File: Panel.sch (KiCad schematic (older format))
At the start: 10 parts, among them J6 Rotated_Barrel, U7 LM3406HV

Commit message: Added Component-Associations (about 10% remaining)
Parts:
- C20: Buy https://www.digikey.com/product-detail/en/samsung-electro-m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 -> (none)
- C21, C23: Buy https://www.digikey.com/product-detail/en/samsung-electro-m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 -> https://www.digikey.com/product-detail/en/kemet/C0603C104M5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
- C22: Buy https://www.digikey.com/product-detail/en/kemet/C0805C223K5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 -> https://www.digikey.com/product-detail/en/kemet/C0603C223K1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
- R11: Buy https://www.digikey.com/product-detail/en/yageo/RC0805FR-07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 -> https://www.digikey.com/product-detail/en/yageo/RC0603FR-07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
- R12: footprint Resistors_SMD:R_0603 -> Resistors_SMD:R_0805
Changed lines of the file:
@@
 $Descr A4 11693 8268
 encoding utf-8
-Sheet 4 7
+Sheet 3 7
 Title ""
 Date "2018-02-14"
@@
 AR Path="/5A4C34AF/5A7753B7" Ref="R11"  Part="1"
 AR Path="/5A4C3F5F/5A7753B7" Ref="R13"  Part="1"
-F 0 "R13" V 1430 1300 50  0000 C CNN
+F 0 "R11" V 1430 1300 50  0000 C CNN
 F 1 "162k" V 1350 1300 50  0000 C CNN
 F 2 "Resistors_SMD:R_0603" V 1280 1300 50  0001 C CNN
 F 3 "" H 1350 1300 50  0001 C CNN
-F 4 "https://www.digikey.com/product-detail/en/yageo/RC0805FR-07162KL/311-162KCRCT-ND/730577" V 1350 1300 60  0001 C CNN "Buy"
+F 4 "https://www.digikey.com/product-detail/en/yageo/RC0603FR-07162KL/311-162KHRCT-ND/729922" V 1350 1300 50  0001 C CNN "Buy"
 	1    1350 1300
 	1    0    0    -1
@@
 AR Path="/5A4C34AF/5A77745B" Ref="C21"  Part="1"
 AR Path="/5A4C3F5F/5A77745B" Ref="C25"  Part="1"
-F 0 "C25" H 1510 2220 50  0000 L CNN
+F 0 "C21" H 1510 2220 50  0000 L CNN
 F 1 "100nF" H 1510 2070 50  0000 L CNN
 F 2 "Capacitors_SMD:C_0603" H 1500 2150 50  0001 C CNN
 F 3 "" H 1500 2150 50  0001 C CNN
-F 4 "https://www.digikey.com/product-detail/en/samsung-electro-mechanics/CL21B104KACNNNC/1276-1099-1-ND/3889185" H 1500 2150 60  0001 C CNN "Buy"
+F 4 "https://www.digikey.com/product-detail/en/kemet/C0603C104M5RACTU/399-7845-1-ND/3471568" H 1500 2150 60  0001 C CNN "Buy"
 	1    1500 2150
 	1    0    0    -1
@@
 AR Path="/5A4C34AF/5A777BDD" Ref="#PWR061"  Part="1"
 AR Path="/5A4C3F5F/5A777BDD" Ref="#PWR068"  Part="1"
-F 0 "#PWR068" H 1500 2050 50  0001 C CNN
+F 0 "#PWR061" H 1500 2050 50  0001 C CNN
 F 1 "GND" H 1500 2150 50  0000 C CNN
 F 2 "" H 1500 2300 50  0001 C CNN
@@
 AR Path="/5A4C34AF/5A777CD4" Ref="C23"  Part="1"
 AR Path="/5A4C3F5F/5A777CD4" Ref="C27"  Part="1"
-F 0 "C27" H 2710 2220 50  0000 L CNN
+F 0 "C23" H 2710 2220 50  0000 L CNN
 F 1 "100nF" H 2710 2070 50  0000 L CNN
 F 2 "Capacitors_SMD:C_0603" H 2700 2150 50  0001 C CNN
 F 3 "" H 2700 2150 50  0001 C CNN
-F 4 "https://www.digikey.com/product-detail/en/samsung-electro-mechanics/CL21B104KACNNNC/1276-1099-1-ND/3889185" H 2700 2150 60  0001 C CNN "Buy"
+F 4 "https://www.digikey.com/product-detail/en/kemet/C0603C104M5RACTU/399-7845-1-ND/3471568" H 2700 2150 50  0001 C CNN "Buy"
 	1    2700 2150
 	1    0    0    -1
@@
 AR Path="/5A4C34AF/5A777CDA" Ref="#PWR063"  Part="1"
 AR Path="/5A4C3F5F/5A777CDA" Ref="#PWR070"  Part="1"
-F 0 "#PWR070" H 2700 2050 50  0001 C CNN
+F 0 "#PWR063" H 2700 2050 50  0001 C CNN
 F 1 "GND" H 2700 2150 50  0000 C CNN
 F 2 "" H 2700 2300 50  0001 C CNN
@@
 AR Path="/5A4C34AF/5A777FA3" Ref="#PWR062"  Part="1"
 AR Path="/5A4C3F5F/5A777FA3" Ref="#PWR069"  Part="1"
-F 0 "#PWR069" H 2100 2050 50  0001 C CNN
+F 0 "#PWR062" H 2100 2050 50  0001 C CNN
 F 1 "GND" H 2100 2150 50  0000 C CNN
 F 2 "" H 2100 2300 50  0001 C CNN
@@
 AR Path="/5A4C34AF/5A77816D" Ref="C22"  Part="1"
 AR Path="/5A4C3F5F/5A77816D" Ref="C26"  Part="1"
-F 0 "C26" H 2460 920 50  0000 L CNN
+F 0 "C22" H 2460 920 50  0000 L CNN
 F 1 "22nF" H 2460 770 50  0000 L CNN
 F 2 "Capacitors_SMD:C_0603" H 2450 850 50  0001 C CNN
 F 3 "" H 2450 850 50  0001 C CNN
-F 4 "https://www.digikey.com/product-detail/en/kemet/C0805C223K5RACTU/399-1163-1-ND/411438" H 2450 850 60  0001 C CNN "Buy"
+F 4 "https://www.digikey.com/product-detail/en/kemet/C0603C223K1RACTU/399-3476-1-ND/754769" H 2450 850 50  0001 C CNN "Buy"
 	1    2450 850
 	0    -1   -1   0
@@
 AR Path="/5A4C34AF/5A77899A" Ref="L3"  Part="1"
 AR Path="/5A4C3F5F/5A77899A" Ref="L4"  Part="1"
-F 0 "L4" V 3200 1050 50  0000 C CNN
+F 0 "L3" V 3200 1050 50  0000 C CNN
 F 1 "33μH" V 3325 1050 50  0000 C CNN
 F 2 "" H 3250 1050 50  0001 C CNN
@@
 AR Path="/5A4C34AF/5A7789F9" Ref="D1"  Part="1"
 AR Path="/5A4C3F5F/5A7789F9" Ref="D2"  Part="1"
-F 0 "D2" H 3000 1400 50  0000 C CNN
+F 0 "D1" H 3000 1400 50  0000 C CNN
 F 1 "D_Schot" H 2950 1200 50  0000 C CNN
 F 2 "Diodes_SMD:D_SOD-123" H 3000 1300 50  0001 C CNN
@@
 AR Path="/5A4C34AF/5A778B62" Ref="#PWR064"  Part="1"
 AR Path="/5A4C3F5F/5A778B62" Ref="#PWR071"  Part="1"
-F 0 "#PWR071" H 3000 2050 50  0001 C CNN
+F 0 "#PWR064" H 3000 2050 50  0001 C CNN
 F 1 "GND" H 3000 2150 50  0000 C CNN
 F 2 "" H 3000 2300 50  0001 C CNN
@@
 AR Path="/5A4C34AF/5A779AD3" Ref="J6"  Part="1"
 AR Path="/5A4C3F5F/5A779AD3" Ref="J7"  Part="1"
-F 0 "J7" H 3700 1710 50  0000 C CNN
+F 0 "J6" H 3700 1710 50  0000 C CNN
 F 1 "Rotated_Barrel" H 3750 1350 50  0000 C CNN
 F 2 "Connectors:BARREL_JACK" H 3750 1440 50  0001 C CNN
@@
 AR Path="/5A4C34AF/5A77A2E1" Ref="R12"  Part="1"
 AR Path="/5A4C3F5F/5A77A2E1" Ref="R14"  Part="1"
-F 0 "R14" V 3530 1900 50  0000 C CNN
+F 0 "R12" V 3530 1900 50  0000 C CNN
 F 1 "0R16" V 3450 1900 50  0000 C CNN
-F 2 "Resistors_SMD:R_0603" V 3380 1900 50  0001 C CNN
+F 2 "Resistors_SMD:R_0805" V 3380 1900 50  0001 C CNN
 F 3 "" H 3450 1900 50  0001 C CNN
 F 4 "https://www.digikey.com/product-detail/en/panasonic-electronic-components/ERJ-6DSFR16V/P19313CT-ND/6004668" V 3450 1900 60  0001 C CNN "Buy"
@@
 AR Path="/5A4C34AF/5A77A9CB" Ref="#PWR065"  Part="1"
 AR Path="/5A4C3F5F/5A77A9CB" Ref="#PWR072"  Part="1"
-F 0 "#PWR072" H 3450 2050 50  0001 C CNN
+F 0 "#PWR065" H 3450 2050 50  0001 C CNN
 F 1 "GND" H 3450 2150 50  0000 C CNN
 F 2 "" H 3450 2300 50  0001 C CNN
@@
 AR Path="/5A4C34AF/5A77D10E" Ref="C20"  Part="1"
 AR Path="/5A4C3F5F/5A77D10E" Ref="C24"  Part="1"
-F 0 "C24" H 1110 1370 50  0000 L CNN
+F 0 "C20" H 1110 1370 50  0000 L CNN
 F 1 "1μF" H 1110 1220 50  0000 L CNN
 F 2 "Capacitors_SMD:C_0603" H 1100 1300 50  0001 C CNN
 F 3 "" H 1100 1300 50  0001 C CNN
-F 4 "https://www.digikey.com/product-detail/en/samsung-electro-mechanics/CL31B105KCHNNNE/1276-1838-1-ND/3889924" H 1100 1300 60  0001 C CNN "Buy"
 	1    1100 1300
 	1    0    0    -1
@@
 AR Path="/5A4C34AF/5A77D43C" Ref="#PWR060"  Part="1"
 AR Path="/5A4C3F5F/5A77D43C" Ref="#PWR067"  Part="1"
-F 0 "#PWR067" H 1100 2050 50  0001 C CNN
+F 0 "#PWR060" H 1100 2050 50  0001 C CNN
 F 1 "GND" H 1100 2150 50  0000 C CNN
 F 2 "" H 1100 2300 50  0001 C CNN
@@
 AR Path="/5A4C34AF/5A77E620" Ref="U7"  Part="1"
 AR Path="/5A4C3F5F/5A77E620" Ref="U8"  Part="1"
-F 0 "U8" H 2500 950 60  0000 C CNN
+F 0 "U7" H 2500 950 60  0000 C CNN
 F 1 "LM3406HV" H 1900 2050 60  0000 C CNN
 F 2 "Housings_SSOP:TSSOP-14_4.4x5mm_Pitch0.65mm" H 2100 2100 60  0001 C CNN
@@
 AR Path="/5A4C34AF/5A84C99A" Ref="#PWR059"  Part="1"
 AR Path="/5A4C3F5F/5A84C99A" Ref="#PWR066"  Part="1"
-F 0 "#PWR066" H 1050 800 50  0001 C CNN
+F 0 "#PWR059" H 1050 800 50  0001 C CNN
 F 1 "+48V" H 1050 1090 50  0000 C CNN
 F 2 "" H 1050 950 50  0001 C CNN

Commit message: Minor changes to layout and component association
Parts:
- C21, C23: Buy https://www.digikey.com/product-detail/en/kemet/C0603C104M5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 -> https://www.digikey.com/product-detail/en/kemet/C0603C104K3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
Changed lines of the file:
@@
 F 2 "Capacitors_SMD:C_0603" H 1500 2150 50  0001 C CNN
 F 3 "" H 1500 2150 50  0001 C CNN
-F 4 "https://www.digikey.com/product-detail/en/kemet/C0603C104M5RACTU/399-7845-1-ND/3471568" H 1500 2150 60  0001 C CNN "Buy"
+F 4 "https://www.digikey.com/product-detail/en/kemet/C0603C104K3RACTU/399-1281-1-ND/416057" H 1500 2150 60  0001 C CNN "Buy"
 	1    1500 2150
 	1    0    0    -1
@@
 F 2 "Capacitors_SMD:C_0603" H 2700 2150 50  0001 C CNN
 F 3 "" H 2700 2150 50  0001 C CNN
-F 4 "https://www.digikey.com/product-detail/en/kemet/C0603C104M5RACTU/399-7845-1-ND/3471568" H 2700 2150 50  0001 C CNN "Buy"
+F 4 "https://www.digikey.com/product-detail/en/kemet/C0603C104K3RACTU/399-1281-1-ND/416057" H 2700 2150 50  0001 C CNN "Buy"
 	1    2700 2150
 	1    0    0    -1

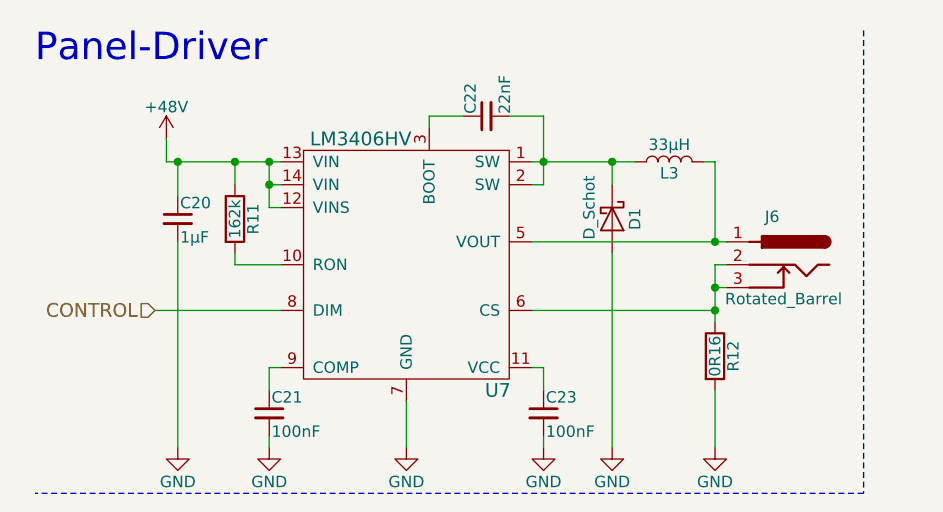
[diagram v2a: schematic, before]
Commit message: Added about 8% of the remaining components
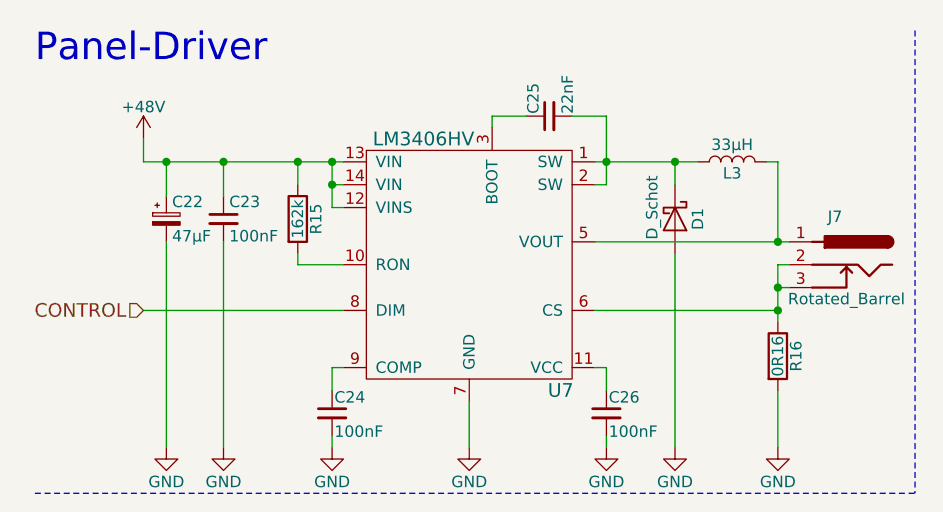
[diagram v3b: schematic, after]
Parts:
- removed C20: 1μF, Capacitors_SMD:C_0603, symbol Device:C_Small
- added C22: 47μF, symbol Device:CP_Small
- added C23: 100nF, Capacitor_SMD:C_0805_2012Metric, symbol Device:C_Small
- D1: footprint Diodes_SMD:D_SOD-123 -> Diode_SMD:D_SMA_Handsoldering; Buy https://www.digikey.com/product-detail/en/nexperia-usa-inc/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 -> https://www.digikey.com/product-detail/en/smc-diode-solutio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
- renumbered C21 to C24, C22 to C25, C23 to C26, J6 to J7, R11 to R15, R12 to R16
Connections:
- net +48V: now also C22.1, C23.1
- net GND: now also C22.2, C23.2
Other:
- moved on the sheet: C24, C25, C26, D1, J7, L3, R15, R16, U7

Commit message: Added Gate Pull-Downs
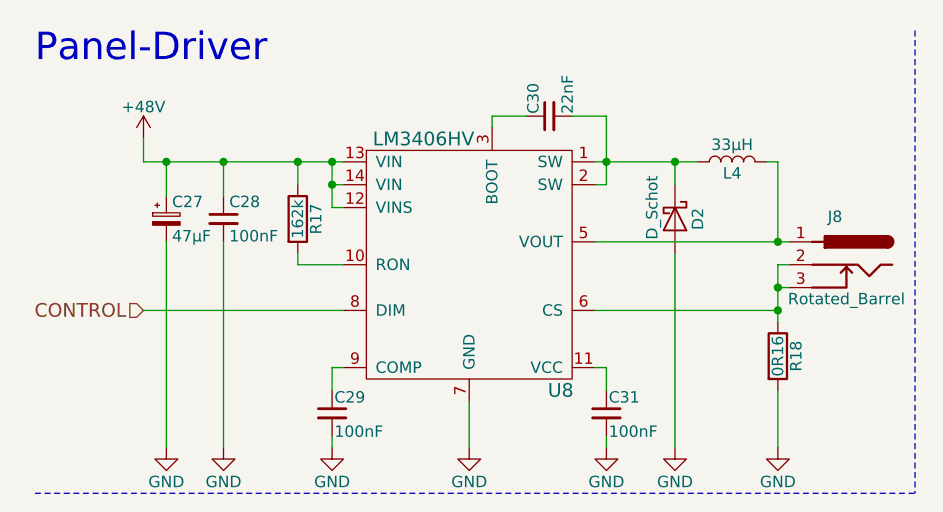
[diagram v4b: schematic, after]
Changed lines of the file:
@@
 $Descr A4 11693 8268
 encoding utf-8
-Sheet 3 7
+Sheet 4 7
 Title ""
 Date "2018-02-14"
@@
 AR Path="/5A4C34AF/5A7753B7" Ref="R15"  Part="1"
 AR Path="/5A4C3F5F/5A7753B7" Ref="R17"  Part="1"
-F 0 "R15" V 1705 1300 50  0000 C CNN
+F 0 "R17" V 1705 1300 50  0000 C CNN
 F 1 "162k" V 1625 1300 50  0000 C CNN
 F 2 "Resistors_SMD:R_0603" V 1555 1300 50  0001 C CNN
@@
 AR Path="/5A4C34AF/5A77745B" Ref="C24"  Part="1"
 AR Path="/5A4C3F5F/5A77745B" Ref="C29"  Part="1"
-F 0 "C24" H 1785 2220 50  0000 L CNN
+F 0 "C29" H 1785 2220 50  0000 L CNN
 F 1 "100nF" H 1785 2070 50  0000 L CNN
 F 2 "Capacitors_SMD:C_0603" H 1775 2150 50  0001 C CNN
@@
 AR Path="/5A4C34AF/5A777BDD" Ref="#PWR063"  Part="1"
 AR Path="/5A4C3F5F/5A777BDD" Ref="#PWR071"  Part="1"
-F 0 "#PWR063" H 1775 2050 50  0001 C CNN
+F 0 "#PWR071" H 1775 2050 50  0001 C CNN
 F 1 "GND" H 1775 2150 50  0000 C CNN
 F 2 "" H 1775 2300 50  0001 C CNN
@@
 AR Path="/5A4C34AF/5A777CD4" Ref="C26"  Part="1"
 AR Path="/5A4C3F5F/5A777CD4" Ref="C31"  Part="1"
-F 0 "C26" H 2985 2220 50  0000 L CNN
+F 0 "C31" H 2985 2220 50  0000 L CNN
 F 1 "100nF" H 2985 2070 50  0000 L CNN
 F 2 "Capacitors_SMD:C_0603" H 2975 2150 50  0001 C CNN
@@
 AR Path="/5A4C34AF/5A777CDA" Ref="#PWR065"  Part="1"
 AR Path="/5A4C3F5F/5A777CDA" Ref="#PWR073"  Part="1"
-F 0 "#PWR065" H 2975 2050 50  0001 C CNN
+F 0 "#PWR073" H 2975 2050 50  0001 C CNN
 F 1 "GND" H 2975 2150 50  0000 C CNN
 F 2 "" H 2975 2300 50  0001 C CNN
@@
 AR Path="/5A4C34AF/5A777FA3" Ref="#PWR064"  Part="1"
 AR Path="/5A4C3F5F/5A777FA3" Ref="#PWR072"  Part="1"
-F 0 "#PWR064" H 2375 2050 50  0001 C CNN
+F 0 "#PWR072" H 2375 2050 50  0001 C CNN
 F 1 "GND" H 2375 2150 50  0000 C CNN
 F 2 "" H 2375 2300 50  0001 C CNN
@@
 AR Path="/5A4C34AF/5A77816D" Ref="C25"  Part="1"
 AR Path="/5A4C3F5F/5A77816D" Ref="C30"  Part="1"
-F 0 "C25" H 2735 920 50  0000 L CNN
+F 0 "C30" H 2735 920 50  0000 L CNN
 F 1 "22nF" H 2735 770 50  0000 L CNN
 F 2 "Capacitors_SMD:C_0603" H 2725 850 50  0001 C CNN
@@
 AR Path="/5A4C34AF/5A77899A" Ref="L3"  Part="1"
 AR Path="/5A4C3F5F/5A77899A" Ref="L4"  Part="1"
-F 0 "L3" V 3475 1050 50  0000 C CNN
+F 0 "L4" V 3475 1050 50  0000 C CNN
 F 1 "33μH" V 3600 1050 50  0000 C CNN
 F 2 "" H 3525 1050 50  0001 C CNN
@@
 AR Path="/5A4C34AF/5A7789F9" Ref="D1"  Part="1"
 AR Path="/5A4C3F5F/5A7789F9" Ref="D2"  Part="1"
-F 0 "D1" H 3275 1400 50  0000 C CNN
+F 0 "D2" H 3275 1400 50  0000 C CNN
 F 1 "D_Schot" H 3225 1200 50  0000 C CNN
 F 2 "Diode_SMD:D_SMA_Handsoldering" H 3275 1300 50  0001 C CNN
@@
 AR Path="/5A4C34AF/5A778B62" Ref="#PWR066"  Part="1"
 AR Path="/5A4C3F5F/5A778B62" Ref="#PWR074"  Part="1"
-F 0 "#PWR066" H 3275 2050 50  0001 C CNN
+F 0 "#PWR074" H 3275 2050 50  0001 C CNN
 F 1 "GND" H 3275 2150 50  0000 C CNN
 F 2 "" H 3275 2300 50  0001 C CNN
@@
 AR Path="/5A4C34AF/5A779AD3" Ref="J7"  Part="1"
 AR Path="/5A4C3F5F/5A779AD3" Ref="J8"  Part="1"
-F 0 "J7" H 3975 1710 50  0000 C CNN
+F 0 "J8" H 3975 1710 50  0000 C CNN
 F 1 "Rotated_Barrel" H 4025 1350 50  0000 C CNN
 F 2 "Connectors:BARREL_JACK" H 4025 1440 50  0001 C CNN
@@
 AR Path="/5A4C34AF/5A77A2E1" Ref="R16"  Part="1"
 AR Path="/5A4C3F5F/5A77A2E1" Ref="R18"  Part="1"
-F 0 "R16" V 3805 1900 50  0000 C CNN
+F 0 "R18" V 3805 1900 50  0000 C CNN
 F 1 "0R16" V 3725 1900 50  0000 C CNN
 F 2 "Resistors_SMD:R_0805" V 3655 1900 50  0001 C CNN
@@
 AR Path="/5A4C34AF/5A77A9CB" Ref="#PWR067"  Part="1"
 AR Path="/5A4C3F5F/5A77A9CB" Ref="#PWR075"  Part="1"
-F 0 "#PWR067" H 3725 2050 50  0001 C CNN
+F 0 "#PWR075" H 3725 2050 50  0001 C CNN
 F 1 "GND" H 3725 2150 50  0000 C CNN
 F 2 "" H 3725 2300 50  0001 C CNN
@@
 AR Path="/5A4C34AF/5A77D43C" Ref="#PWR062"  Part="1"
 AR Path="/5A4C3F5F/5A77D43C" Ref="#PWR070"  Part="1"
-F 0 "#PWR062" H 1300 2050 50  0001 C CNN
+F 0 "#PWR070" H 1300 2050 50  0001 C CNN
 F 1 "GND" H 1300 2150 50  0000 C CNN
 F 2 "" H 1300 2300 50  0001 C CNN
@@
 AR Path="/5A4C34AF/5A77E620" Ref="U7"  Part="1"
 AR Path="/5A4C3F5F/5A77E620" Ref="U8"  Part="1"
-F 0 "U7" H 2775 950 60  0000 C CNN
+F 0 "U8" H 2775 950 60  0000 C CNN
 F 1 "LM3406HV" H 2175 2050 60  0000 C CNN
 F 2 "Housings_SSOP:TSSOP-14_4.4x5mm_Pitch0.65mm" H 2375 2100 60  0001 C CNN
@@
 AR Path="/5A4C34AF/5A84C99A" Ref="#PWR060"  Part="1"
 AR Path="/5A4C3F5F/5A84C99A" Ref="#PWR068"  Part="1"
-F 0 "#PWR060" H 950 800 50  0001 C CNN
+F 0 "#PWR068" H 950 800 50  0001 C CNN
 F 1 "+48V" H 950 1090 50  0000 C CNN
 F 2 "" H 950 950 50  0001 C CNN
@@
 AR Path="/5A4C34AF/5ABA3DDA" Ref="C22"  Part="1"
 AR Path="/5A4C3F5F/5ABA3DDA" Ref="C27"  Part="1"
-F 0 "C22" H 1075 1375 50  0000 L CNN
+F 0 "C27" H 1075 1375 50  0000 L CNN
 F 1 "47μF" H 1075 1225 50  0000 L CNN
 F 2 "" H 1050 1300 50  0001 C CNN
@@
 AR Path="/5A4C34AF/5ABA5E6C" Ref="C23"  Part="1"
 AR Path="/5A4C3F5F/5ABA5E6C" Ref="C28"  Part="1"
-F 0 "C23" H 1325 1375 50  0000 L CNN
+F 0 "C28" H 1325 1375 50  0000 L CNN
 F 1 "100nF" H 1325 1225 50  0000 L CNN
 F 2 "Capacitor_SMD:C_0805_2012Metric" H 1300 1300 50  0001 C CNN
@@
 AR Path="/5A4C34AF/5ABA815F" Ref="#PWR061"  Part="1"
 AR Path="/5A4C3F5F/5ABA815F" Ref="#PWR069"  Part="1"
-F 0 "#PWR061" H 1050 2050 50  0001 C CNN
+F 0 "#PWR069" H 1050 2050 50  0001 C CNN
 F 1 "GND" H 1050 2150 50  0000 C CNN
 F 2 "" H 1050 2300 50  0001 C CNN
